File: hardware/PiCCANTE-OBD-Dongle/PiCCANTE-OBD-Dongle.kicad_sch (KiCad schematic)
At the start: 36 parts, among them J1 Micro_SD_Card, U1 SN65HVD230, U2 SN65HVD230, U3 SN65HVD230, U4 TPS5430DDA

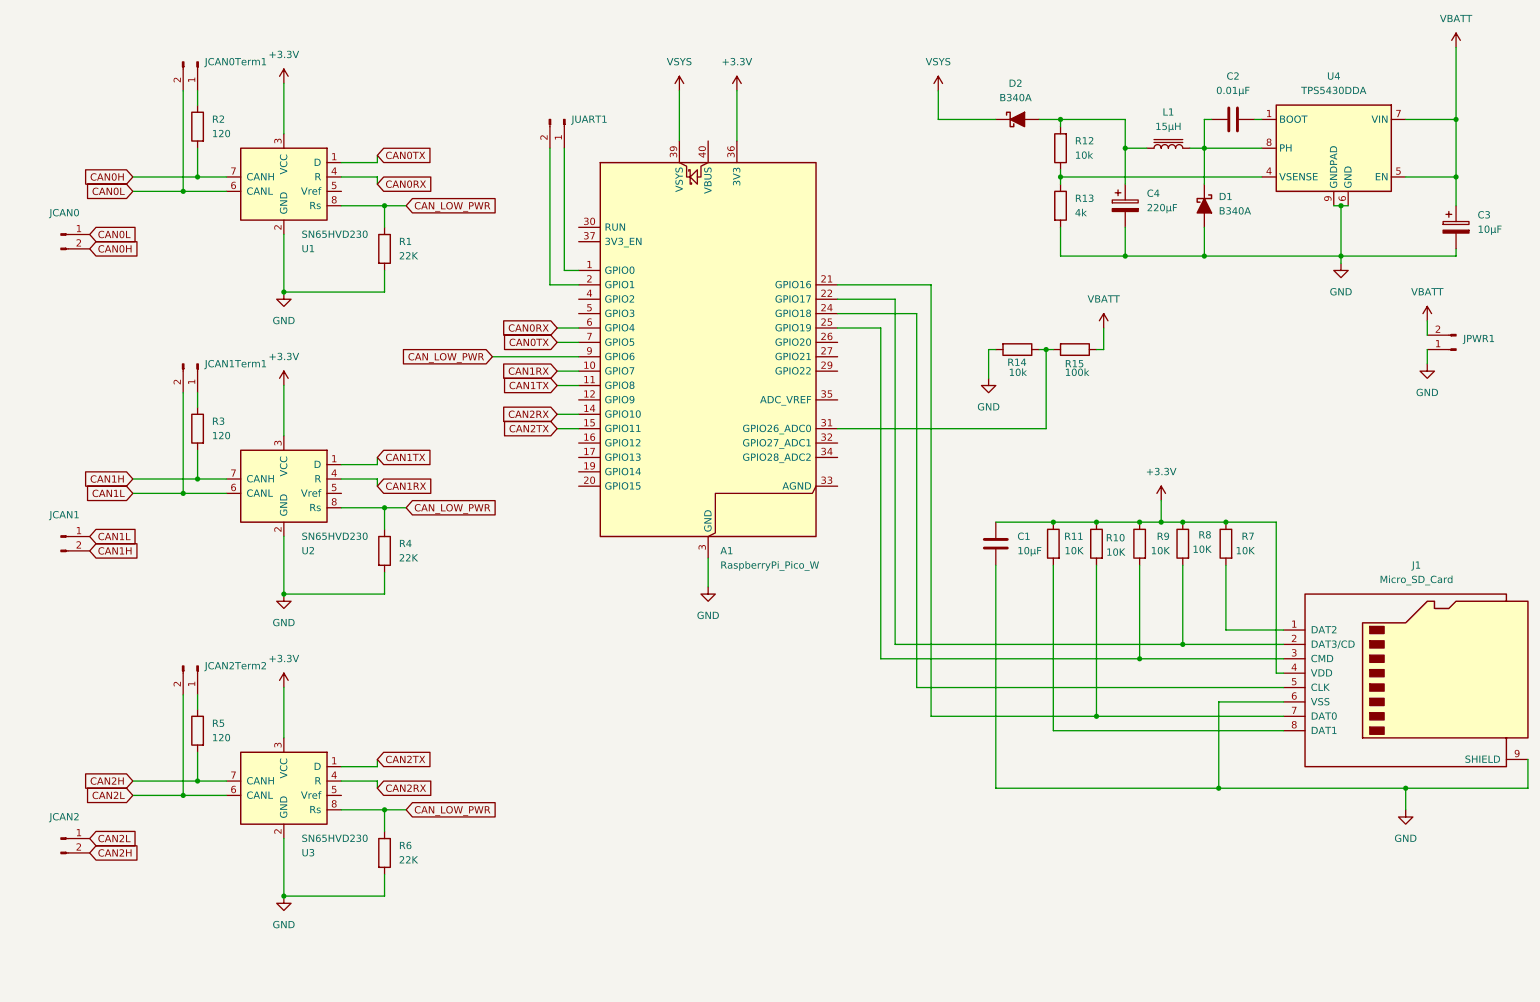
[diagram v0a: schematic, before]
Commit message: Switch out TRX / "Improve" Routing
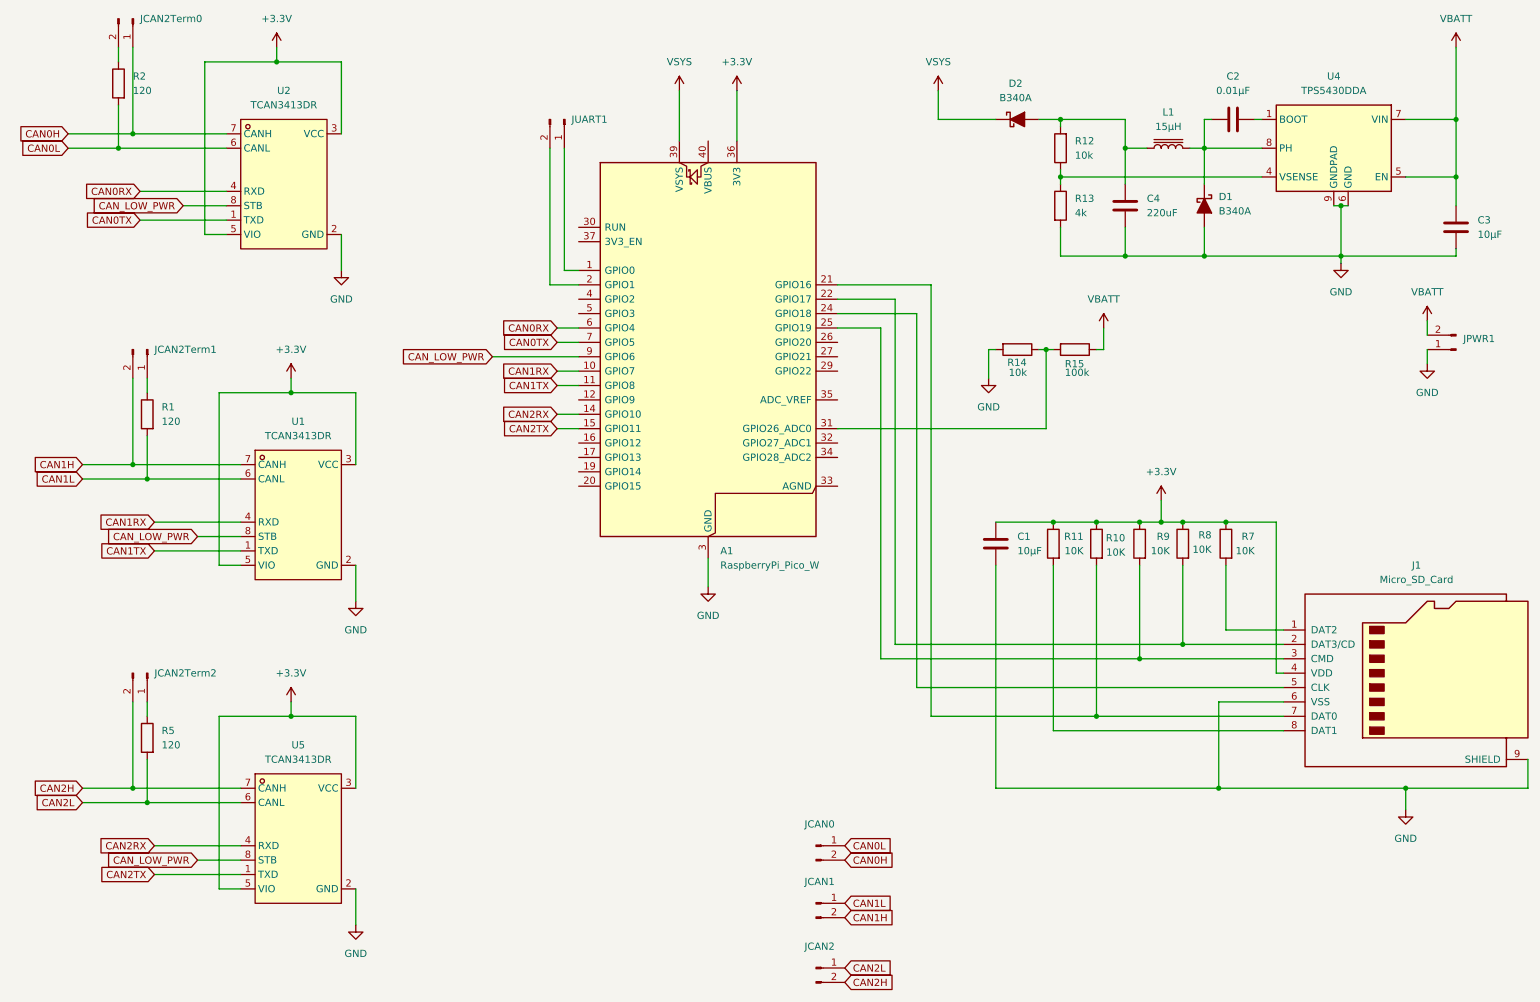
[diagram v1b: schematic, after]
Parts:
- removed C3: 10µF, Capacitor_SMD:CP_Elec_4x5.4, symbol Device:C_Polarized
- removed C4: 220µF, Capacitor_SMD:CP_Elec_6.3x5.4_Nichicon, symbol Device:C_Polarized
- removed JCAN0Term1, JCAN1Term1: ~, Connector_PinHeader_2.54mm:PinHeader_1x02_P2.54mm_Vertical, symbol Connector:Conn_01x02_Pin
- removed R1: 22K, PCM_Resistor_SMD_AKL:R_0201_0603Metric, symbol Device:R
- removed R3: 120, PCM_Resistor_SMD_AKL:R_0201_0603Metric, symbol PCM_Resistor_AKL:R_0805
- removed R4, R6: 22K, Resistor_SMD:R_0201_0603Metric, symbol Device:R
- removed U1, U2, U3: SN65HVD230, Package_SO:SOIC-8_3.9x4.9mm_P1.27mm, symbol Interface_CAN_LIN:SN65HVD230
- added C3: 10µF, PCM_Capacitor_SMD_AKL:C_1206_3216Metric, symbol Device:C
- added C4: 220uF, PCM_Capacitor_SMD_AKL:C_1206_3216Metric, symbol Device:C
- added JCAN2Term0, JCAN2Term1: ~, Connector_PinHeader_2.54mm:PinHeader_1x02_P2.54mm_Vertical, symbol Connector:Conn_01x02_Pin
- added R1: 120, PCM_Resistor_SMD_AKL:R_0201_0603Metric, symbol PCM_Resistor_AKL:R_0805
- added U1, U2, U5: TCAN3413DR, EasyEDA:SOP-8_L4.9-W3.9-P1.27-LS6.0-BL-1, symbol EasyEDA:TCAN3413DR
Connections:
- net +3.3V: now also U1.3 (VCC), U1.5 (VIO), U2.3 (VCC), U2.5 (VIO), U5.3 (VCC), U5.5 (VIO)
- net CAN0H: now also JCAN2Term0.1 (Pin_1), U2.7 (CANH); no longer R2.1
- net CAN0L: now also R2.1, U2.6 (CANL)
- net CAN0RX: now also U2.4 (RXD)
- net CAN0TX: now also U2.1 (TXD)
- net CAN1H: now also JCAN2Term1.2 (Pin_2), U1.7 (CANH)
- net CAN1L: now also R1.1, U1.6 (CANL)
- net CAN1RX: now also U1.4 (RXD)
- net CAN1TX: now also U1.1 (TXD)
- net CAN2H: now also JCAN2Term2.2 (Pin_2), U5.7 (CANH); no longer R5.1
- net CAN2L: now also R5.1, U5.6 (CANL); no longer JCAN2Term2.2 (Pin_2)
- net CAN2RX: now also U5.4 (RXD)
- net CAN2TX: now also U5.1 (TXD)
- net CAN_LOW_PWR: now also U1.8 (STB), U2.8 (STB), U5.8 (STB)
- net GND: now also C3.2, C4.2, U1.2 (GND), U2.2 (GND), U5.2 (GND)
- net VBATT: now also C3.1
- net at D2.2 (A), L1.1, R12.2: now also C4.1
- net at R2.2: now also JCAN2Term0.2 (Pin_2)
- new net: JCAN2Term1.1 (Pin_1), R1.2
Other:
- moved on the sheet: JCAN0, JCAN1, JCAN2, JCAN2Term2, R5

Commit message: Put pico on the other side
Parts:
- A1: footprint PiCO_CUSTOM_KEEPOUT:RaspberryPi_Pico_W_SMD_HandSolder_CUSTOM_KEEPOUT -> PiCO_CUSTOM_KEEPOUT:RaspberryPi_Pico_W_SMD_THT_COMBO_CUSTOM_KEEPOUT
- C1, C2: footprint PCM_Capacitor_SMD_AKL:C_0201_0603Metric -> Capacitor_SMD:C_0603_1608Metric
- C3, C4: footprint PCM_Capacitor_SMD_AKL:C_1206_3216Metric -> Capacitor_SMD:C_1206_3216Metric
- JCAN0, JCAN1, JCAN2: footprint Connector_PinHeader_2.54mm:PinHeader_1x02_P2.54mm_Horizontal -> Connector_PinHeader_2.54mm:PinHeader_1x02_P2.54mm_Vertical
- L1: footprint Inductor_SMD:L_6.3x6.3_H3 -> EasyEDA:IND-SMD_L4.0-W4.0
- R1, R10, R11, R2, R5, R7, R8, R9: footprint PCM_Resistor_SMD_AKL:R_0201_0603Metric -> Resistor_SMD:R_0603_1608Metric
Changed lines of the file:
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@@
 			)
 		)
-		(property "Footprint" "Inductor_SMD:L_6.3x6.3_H3"
+		(property "Footprint" "EasyEDA:IND-SMD_L4.0-W4.0"
 			(at 217.17 41.91 0)
 			(effects
@@
 			)
 		)
-		(property "Footprint" "PCM_Resistor_SMD_AKL:R_0201_0603Metric"
+		(property "Footprint" "Resistor_SMD:R_0603_1608Metric"
 			(at 31.75 19.05 0)
 			(effects
@@
 			)
 		)
-		(property "Footprint" "Connector_PinHeader_2.54mm:PinHeader_1x02_P2.54mm_Horizontal"
+		(property "Footprint" "Connector_PinHeader_2.54mm:PinHeader_1x02_P2.54mm_Vertical"
 			(at 154.94 175.26 0)
 			(effects
@@
 			)
 		)
-		(property "Footprint" "Connector_PinHeader_2.54mm:PinHeader_1x02_P2.54mm_Horizontal"
+		(property "Footprint" "Connector_PinHeader_2.54mm:PinHeader_1x02_P2.54mm_Vertical"
 			(at 154.94 165.1 0)
 			(effects
@@
 			)
 		)
-		(property "Footprint" "PCM_Capacitor_SMD_AKL:C_1206_3216Metric"
+		(property "Footprint" "Capacitor_SMD:C_1206_3216Metric"
 			(at 210.5152 55.88 0)
 			(effects
@@
 			)
 		)
-		(property "Footprint" "PCM_Resistor_SMD_AKL:R_0201_0603Metric"
+		(property "Footprint" "Resistor_SMD:R_0603_1608Metric"
 			(at 221.488 111.76 90)
 			(effects
@@
 			)
 		)
-		(property "Footprint" "PCM_Resistor_SMD_AKL:R_0201_0603Metric"
+		(property "Footprint" "Resistor_SMD:R_0603_1608Metric"
 			(at 213.868 111.76 90)
 			(effects
@@
 			)
 		)
-		(property "Footprint" "PCM_Capacitor_SMD_AKL:C_0201_0603Metric"
+		(property "Footprint" "Capacitor_SMD:C_0603_1608Metric"
 			(at 187.6552 115.57 0)
 			(effects
@@
 			)
 		)
-		(property "Footprint" "PCM_Resistor_SMD_AKL:R_0201_0603Metric"
+		(property "Footprint" "Resistor_SMD:R_0603_1608Metric"
 			(at 36.83 134.62 0)
 			(effects
@@
 			)
 		)
-		(property "Footprint" "PCM_Capacitor_SMD_AKL:C_0201_0603Metric"
+		(property "Footprint" "Capacitor_SMD:C_0603_1608Metric"
 			(at 224.79 37.7952 0)
 			(effects
@@
 			)
 		)
-		(property "Footprint" "PCM_Resistor_SMD_AKL:R_0201_0603Metric"
+		(property "Footprint" "Resistor_SMD:R_0603_1608Metric"
 			(at 206.248 111.76 90)
 			(effects
@@
 			)
 		)
-		(property "Footprint" "PiCO_CUSTOM_KEEPOUT:RaspberryPi_Pico_W_SMD_HandSolder_CUSTOM_KEEPOUT"
+		(property "Footprint" "PiCO_CUSTOM_KEEPOUT:RaspberryPi_Pico_W_SMD_THT_COMBO_CUSTOM_KEEPOUT"
 			(at 135.89 125.73 0)
 			(effects
@@
 			)
 		)
-		(property "Footprint" "PCM_Resistor_SMD_AKL:R_0201_0603Metric"
+		(property "Footprint" "Resistor_SMD:R_0603_1608Metric"
 			(at 229.108 111.76 90)
 			(effects
@@
 			)
 		)
-		(property "Footprint" "Connector_PinHeader_2.54mm:PinHeader_1x02_P2.54mm_Horizontal"
+		(property "Footprint" "Connector_PinHeader_2.54mm:PinHeader_1x02_P2.54mm_Vertical"
 			(at 154.94 186.69 0)
 			(effects
@@
 			)
 		)
-		(property "Footprint" "PCM_Resistor_SMD_AKL:R_0201_0603Metric"
+		(property "Footprint" "Resistor_SMD:R_0603_1608Metric"
 			(at 36.83 77.47 0)
 			(effects
@@
 			)
 		)
-		(property "Footprint" "PCM_Capacitor_SMD_AKL:C_1206_3216Metric"
+		(property "Footprint" "Capacitor_SMD:C_1206_3216Metric"
 			(at 268.9352 59.69 0)
 			(effects
@@
 			)
 		)
-		(property "Footprint" "PCM_Resistor_SMD_AKL:R_0201_0603Metric"
+		(property "Footprint" "Resistor_SMD:R_0603_1608Metric"
 			(at 198.628 111.76 90)
 			(effects
